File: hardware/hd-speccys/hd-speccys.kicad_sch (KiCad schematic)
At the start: 6 parts, among them J1 PI_ZERO_2x20, J2 ULA_ZX_02x20, J3 ULA_SOCKET_02x20, U1 74LS541, U2 74LS132, U3 74LS541

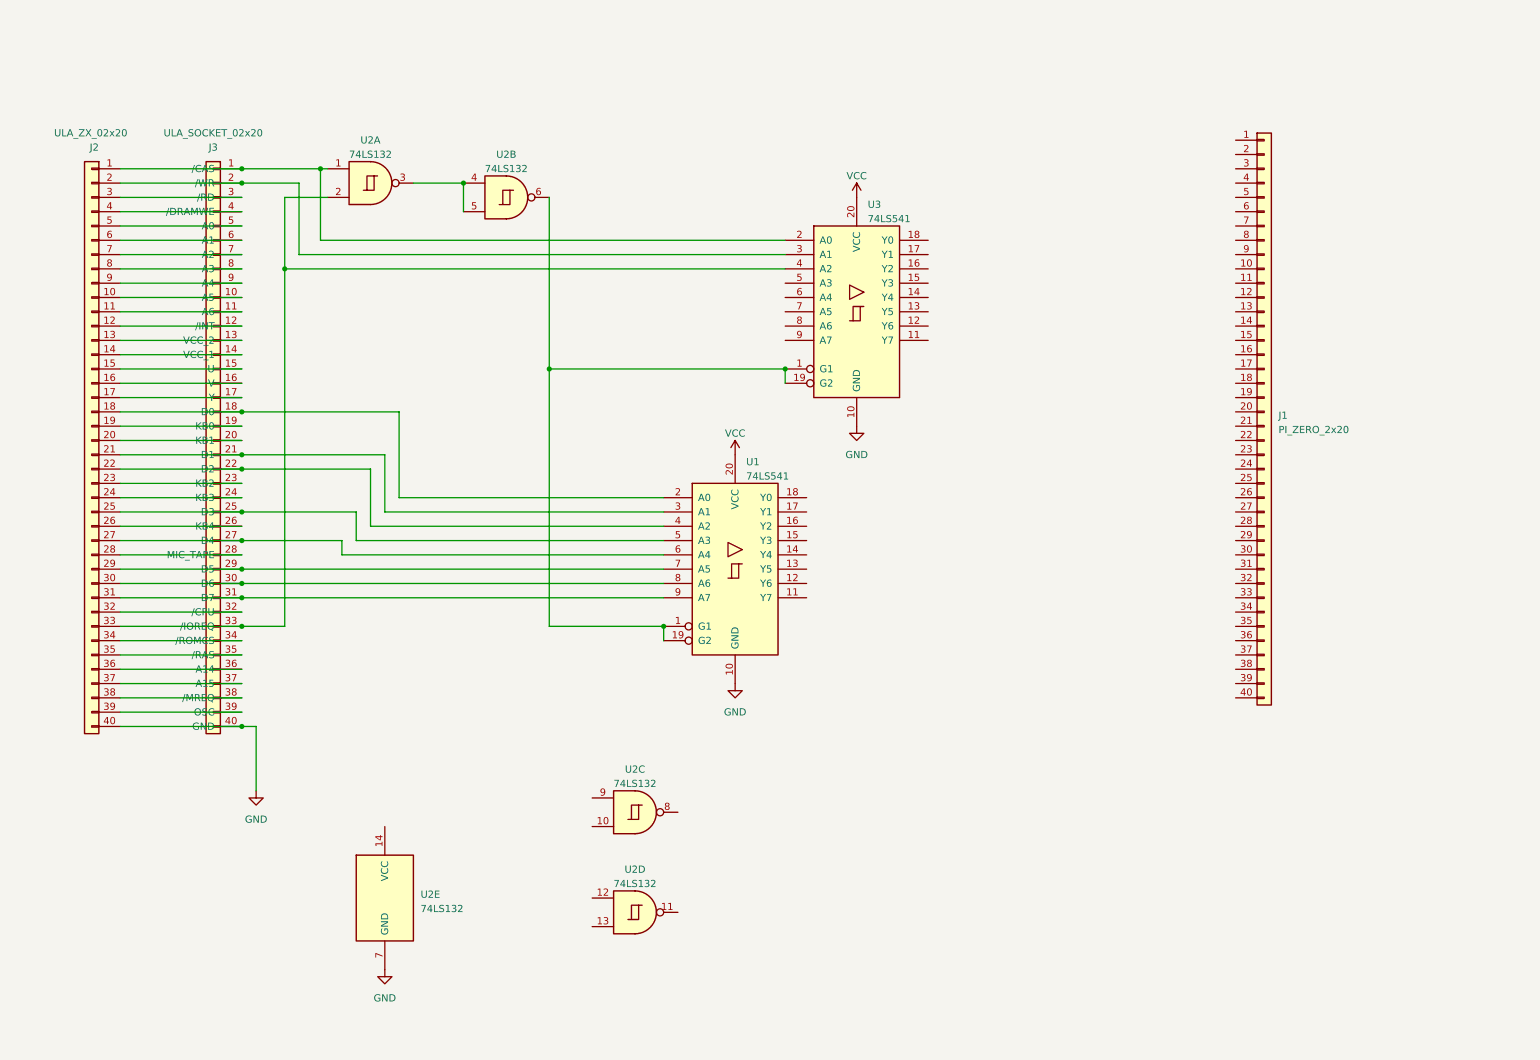
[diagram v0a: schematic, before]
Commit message: WE HAVE VIDEO (albeit quite corrupted!)
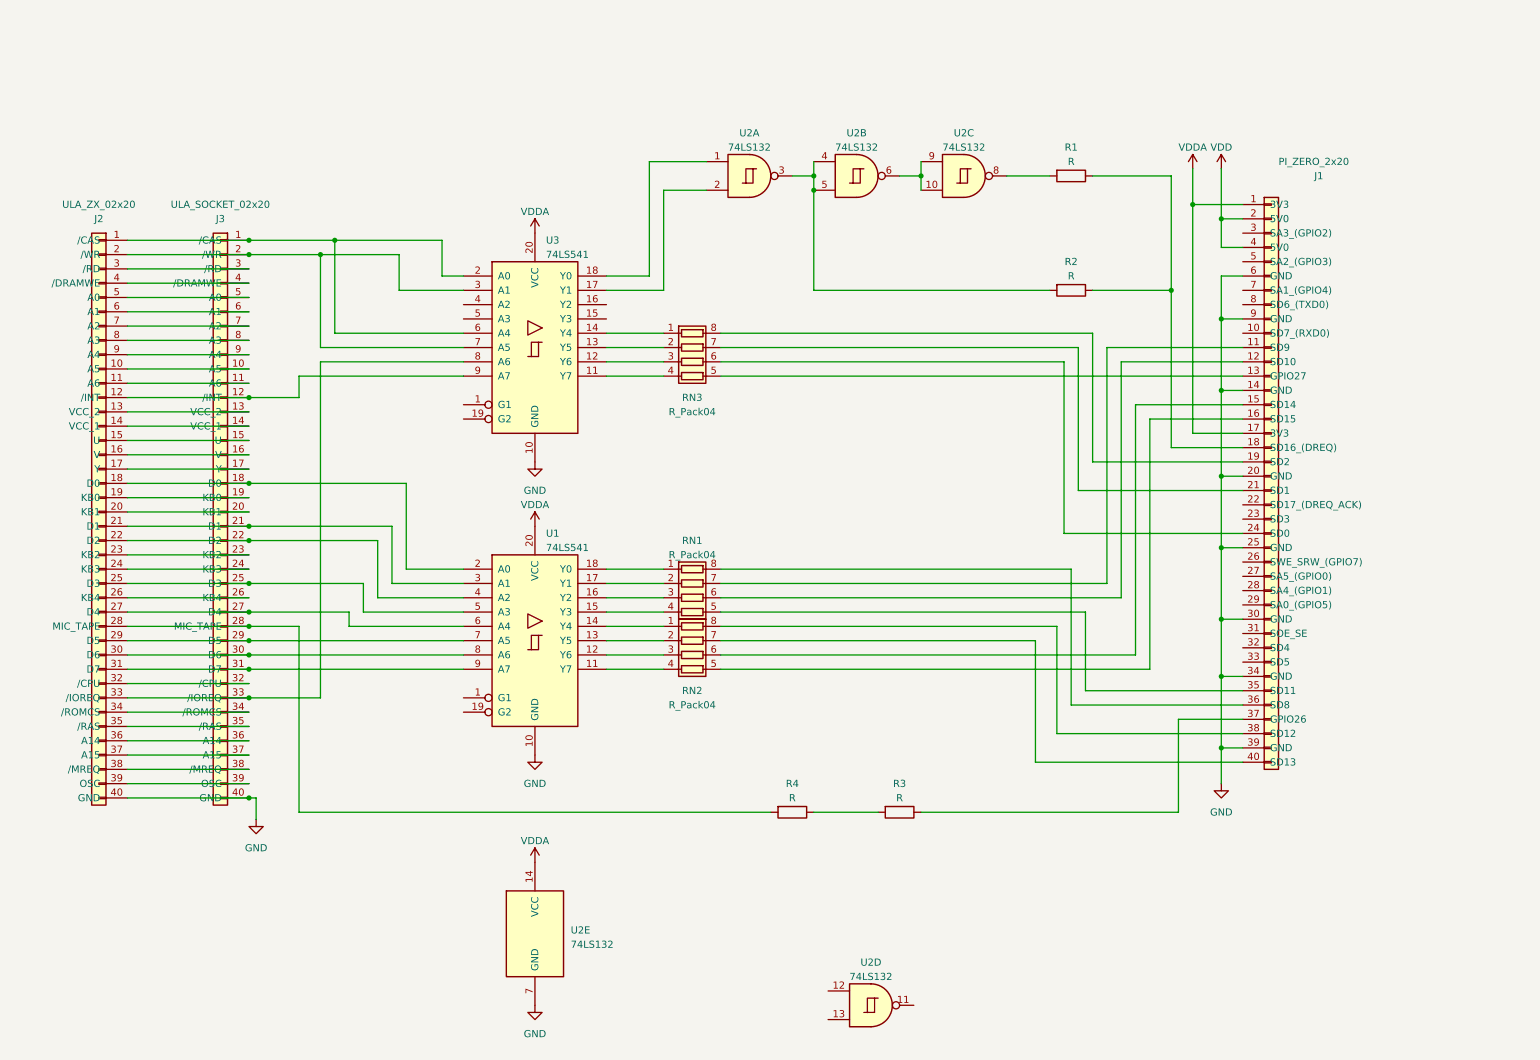
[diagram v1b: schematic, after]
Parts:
- added R1, R2, R3, R4: R, symbol Device:R
- added RN1, RN2, RN3: R_Pack04, symbol Device:R_Pack04
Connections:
- net VCC is gone; now on net VDDA: U1.20 (VCC), U3.20 (VCC)
- net GND: now also J1.14 (GND), J1.20 (GND), J1.25 (GND), J1.30 (GND), J1.34 (GND), J1.39 (GND), J1.6 (GND), J1.9 (GND)
- net at U3.11 (Y7): now also RN3.4 (R4.1)
- net at U3.12 (Y6): now also RN3.3 (R3.1)
- net at U3.13 (Y5): now also RN3.2 (R2.1)
- net at U3.14 (Y4): now also RN3.1 (R1.1)
- net at U3.17 (Y1): now also U2.2
- net at U3.18 (Y0): now also U2.1
- net at J2.1 (/CAS), J3.1 (/CAS), U3.2 (A0): now also U3.6 (A4); no longer U2.1
- net at J2.2 (/WR), J3.2 (/WR), U3.3 (A1): now also U3.7 (A5)
- net at J2.33 (/IOREQ), J3.33 (/IOREQ): now also U3.8 (A6); no longer U2.2, U3.4 (A2)
- net at U3.9 (A7): now also J2.12 (/INT), J3.12 (/INT)
- net at J2.28 (MIC_TAPE), J3.28 (MIC_TAPE): now also R4.2
- net at U2.10: now also U2.6, U2.9
- net at U2.8: now also R1.2
- net at U2.3, U2.4, U2.5: now also R2.2
- net VDDA: now reaches U2.14 (VCC)
- net VDDA: now also J1.1 (3V3), J1.17 (3V3)
- net at J1.11 (SD9): now also RN1.7 (R2.2)
- net at J1.12 (SD10): now also RN1.6 (R3.2)
- net at J1.13 (GPIO27): now also RN3.5 (R4.2)
- net at J1.15 (SD14): now also RN2.6 (R3.2)
- net at J1.16 (SD15): now also RN2.5 (R4.2)
- net at J1.18 (SD16_(DREQ)): now also R1.1, R2.1
- net at J1.19 (SD2): now also RN3.8 (R1.2)
- net VDD: now reaches J1.2 (5V0)
- net VDD: now also J1.4 (5V0)
- net at J1.21 (SD1): now also RN3.7 (R2.2)
- net at J1.24 (SD0): now also RN3.6 (R3.2)
- net at J1.35 (SD11): now also RN1.5 (R4.2)
- net at J1.36 (SD8): now also RN1.8 (R1.2)
- net at J1.37 (GPIO26): now also R3.1
- net at J1.38 (SD12): now also RN2.8 (R1.2)
- net at J1.40 (SD13): now also RN2.7 (R2.2)
- net at U1.11 (Y7): now also RN2.4 (R4.1)
- net at U1.12 (Y6): now also RN2.3 (R3.1)
- net at U1.13 (Y5): now also RN2.2 (R2.1)
- net at U1.14 (Y4): now also RN2.1 (R1.1)
- net at U1.15 (Y3): now also RN1.4 (R4.1)
- net at U1.16 (Y2): now also RN1.3 (R3.1)
- net at U1.17 (Y1): now also RN1.2 (R2.1)
- net at U1.18 (Y0): now also RN1.1 (R1.1)
- new net: R3.2, R4.1
- now unconnected: U1.1 (G1), U1.19 (G2), U3.1 (G1), U3.19 (G2)
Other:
- moved on the sheet: J3, U1, U2A, U2B, U2C, U2D, U2E, U3

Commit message: wip: PCB prototype/schematic
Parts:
- removed RN1, RN2, RN3: R_Pack04, symbol Device:R_Pack04
- removed U2: 74LS132, symbol 74xx:74LS132
- added C1: 100nF, Capacitor_SMD:C_0603_1608Metric_Pad1.08x0.95mm_HandSolder, symbol Device:C
- added C2, C3, C4, C5: C, Capacitor_SMD:C_0603_1608Metric_Pad1.08x0.95mm_HandSolder, symbol Device:C
- added D1, D2, D3: 1N4148, Diode_SMD:D_SOD-323_HandSoldering, symbol Diode:1N4148
- added J1: POWER 9-20VDC, Connector_PinHeader_2.54mm:PinHeader_1x02_P2.54mm_Horizontal, symbol Connector:Conn_01x02_Pin
- added J5: UART, Connector_PinHeader_2.54mm:PinHeader_1x03_P2.54mm_Vertical, symbol Connector:Conn_01x03_Pin
- added J6: Debug_Data, Connector_PinHeader_2.54mm:PinHeader_1x08_P2.54mm_Vertical, symbol Connector:Conn_01x08_Pin
- added J7: Debug_Ctrl, Connector_PinHeader_2.54mm:PinHeader_1x06_P2.54mm_Vertical, symbol Connector:Conn_01x06_Pin
- added R1, R10, R11, R12, R13, R14, R15, R16, R17, R18, R19, R2, R20, R21, R22, R23, R24, R25, R26, R27, R28, R3, R31, R34, R35, R5, R6, R7, R8, R9: R, Resistor_SMD:R_0603_1608Metric_Pad0.98x0.95mm_HandSolder, symbol Device:R
- added R32: 1k, Potentiometer_SMD:Potentiometer_Bourns_TC33X_Vertical, symbol Device:R_Variable
- added U3, U5: 74HC00, Package_SO:TSSOP-14_4.4x5mm_P0.65mm, symbol 74xx:74HC00
- added U4: TSR_1-2450, Converter_DCDC:Converter_DCDC_TRACO_TSR-1_THT, symbol Regulator_Switching:TSR_1-2450
- J2: renamed from J1; footprint (none) -> Module:Raspberry_Pi_Zero_Socketed_THT_FaceDown_MountingHoles
- J3: footprint (none) -> Package_DIP:DIP-40_W15.24mm_Socket
- J4: renamed from J2; footprint (none) -> Package_DIP:DIP-40_W15.24mm_Socket
- R29: renamed from R3; footprint (none) -> Resistor_SMD:R_0603_1608Metric_Pad0.98x0.95mm_HandSolder
- R30: renamed from R2; footprint (none) -> Resistor_SMD:R_0603_1608Metric_Pad0.98x0.95mm_HandSolder
- R33: renamed from R1; footprint (none) -> Resistor_SMD:R_0603_1608Metric_Pad0.98x0.95mm_HandSolder
- R4: footprint (none) -> Resistor_SMD:R_0603_1608Metric_Pad0.98x0.95mm_HandSolder
- U1: renamed from U3; footprint (none) -> Package_SO:TSSOP-20_4.4x6.5mm_P0.65mm
- U2: renamed from U1; footprint (none) -> Package_SO:TSSOP-20_4.4x6.5mm_P0.65mm
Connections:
- net GND: now also U1.1 (G1), U1.19 (G2), U2.1 (G1), U2.19 (G2), C2.2, C3.2, C4.2, C5.2, J1.2 (GND), J5.1 (GND), U3.7 (GND), U4.2 (GND), U5.7 (GND)
- net VDD: now also U4.3 (Vout)
- net VDDA: now also C2.1, C3.1, C4.1, C5.1, U3.14 (VCC), U5.14 (VCC)
- net at U1.14 (Y4): now also R18.2
- net at U1.13 (Y5): now also U3.2
- net at U1.12 (Y6): now also R19.2
- net at U1.11 (Y7): now also R20.2
- net at J2.13 (GPIO27): now also J7.1 (Pin_1), R20.1
- net at J2.24 (SD0): now also J7.4 (Pin_4), R19.1
- net at J2.21 (SD1): now also J7.2 (Pin_2), R18.1
- net at J2.19 (SD2): now also J7.3 (Pin_3), R17.1
- net at R29.2: now also J7.5 (Pin_5), U3.3; no longer R4.1
- net at J3.28 (MIC_TAPE), J4.28 (MIC_TAPE): now also C1.2; no longer R4.2
- net at U1.15 (Y3): now also U3.5
- net at U1.16 (Y2): now also R17.2
- net at U1.17 (Y1): now also U3.1
- net at U1.18 (Y0): now also U3.4
- net at J3.1 (/CAS), J4.1 (/CAS): now also R4.2, R5.2; no longer U1.2 (A0), U1.6 (A4)
- net at J3.2 (/WR), J4.2 (/WR): now also R6.2, R7.2; no longer U1.3 (A1), U1.7 (A5)
- net at U1.4 (A2): now also R3.1
- net at U1.5 (A3): now also R4.1
- net at J3.33 (/IOREQ), J4.33 (/IOREQ): now also R1.2, R2.2, R3.2; no longer U1.8 (A6)
- net at J3.12 (/INT), J4.12 (/INT): now also R8.2; no longer U1.9 (A7)
- net at U2.18 (Y0): now also R21.2
- net at U2.17 (Y1): now also R22.2
- net at U2.16 (Y2): now also R23.2
- net at U2.15 (Y3): now also R24.2
- net at J2.35 (SD11): now also J6.5 (Pin_5), R25.1
- net at J2.12 (SD10): now also J6.6 (Pin_6), R26.1
- net at J2.11 (SD9): now also J6.7 (Pin_7), R27.1
- net at J2.36 (SD8): now also J6.8 (Pin_8), R28.1
- net at J3.18 (D0), J4.18 (D0): now also R9.2; no longer U2.2 (A0)
- net at J3.21 (D1), J4.21 (D1): now also R10.2; no longer U2.3 (A1)
- net at J3.22 (D2), J4.22 (D2): now also R11.2; no longer U2.4 (A2)
- net at J3.25 (D3), J4.25 (D3): now also R12.2; no longer U2.5 (A3)
- net at J3.27 (D4), J4.27 (D4): now also R13.2; no longer U2.6 (A4)
- net at J3.29 (D5), J4.29 (D5): now also R14.2; no longer U2.7 (A5)
- net at J3.30 (D6), J4.30 (D6): now also R15.2; no longer U2.8 (A6)
- net at J3.31 (D7), J4.31 (D7): now also R16.2; no longer U2.9 (A7)
- net at J2.18 (SD16_(DREQ)), R30.1, R33.1: now also R34.1, R35.1
- net at R33.2: now also U3.11, U5.1, U5.2
- net at R30.2: now also J7.6 (Pin_6), U3.10, U3.6, U3.9
- net at U2.14 (Y4): now also R25.2
- net at U2.13 (Y5): now also R26.2
- net at U2.12 (Y6): now also R27.2
- net at U2.11 (Y7): now also R28.2
- net at J2.16 (SD15): now also J6.1 (Pin_1), R21.1
- net at J2.15 (SD14): now also J6.2 (Pin_2), R22.1
- net at J2.40 (SD13): now also J6.3 (Pin_3), R23.1
- net at J2.38 (SD12): now also J6.4 (Pin_4), R24.1
- net at J2.10 (SD7_(RXD0)): now also J5.3 (RXD)
- net at J2.26 (SWE_SRW_(GPIO7)): now also D3.2 (A)
- net at J2.8 (SD6_(TXD0)): now also J5.2 (TXD)
- new net: J1.1 (VCC), U4.1 (Vin)
- new net: D2.2 (A), D3.1 (K)
- new net: R6.1, U1.7 (A5)
- new net: R34.2, U5.10, U5.6, U5.9
- new net: U5.12, U5.13, U5.8
- new net: R2.1, U1.3 (A1)
- new net: R35.2, U5.11
- new net: R5.1, U1.6 (A4)
- new net: R10.1, U2.3 (A1)
- new net: R31.1, R32.2
- new net: C1.1, R31.2
- new net: R1.1, U1.2 (A0)
- new net: R7.1, U1.8 (A6)
- new net: R8.1, U1.9 (A7)
- new net: D1.1 (K), R32.1
- new net: R15.1, U2.8 (A6)
- new net: R9.1, U2.2 (A0)
- new net: R16.1, U2.9 (A7)
- new net: U5.3, U5.4, U5.5
- new net: R11.1, U2.4 (A2)
- new net: R14.1, U2.7 (A5)
- new net: R13.1, U2.6 (A4)
- new net: D1.2 (A), D2.1 (K)
- new net: R12.1, U2.5 (A3)
- new net: U3.12, U3.13, U3.8
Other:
- moved on the sheet: J2, J3, J4, R29, R30, R33, U1, U2

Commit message: hw: schematic updates
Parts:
- removed C5: C, Capacitor_SMD:C_0603_1608Metric_Pad1.08x0.95mm_HandSolder, symbol Device:C
- removed R33, R34, R35: R, Resistor_SMD:R_0603_1608Metric_Pad0.98x0.95mm_HandSolder, symbol Device:R
- removed U3, U5: 74HC00, Package_SO:TSSOP-14_4.4x5mm_P0.65mm, symbol 74xx:74HC00
- added U3: 74LS10, Package_SO:TSSOP-14_4.4x5mm_P0.65mm, symbol 74xx:74LS10
- added U5: 74AHC1G32, Package_TO_SOT_SMD:SOT-353_SC-70-5_Handsoldering, symbol 74xGxx:74AHC1G32
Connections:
- net GND: now also U1.2 (A0), U3.7 (GND), U5.3 (GND)
- net VDDA: now also U3.14 (VCC), U5.5 (VCC)
- net at J3.33 (/IOREQ), J4.33 (/IOREQ), R2.2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: no longer R1.2
- net at J2.18 (SD16_(DREQ)), R30.1: now also J7.1 (Pin_1), R1.1
- net at J2.13 (GPIO27), R20.1: now also J7.6 (Pin_6); no longer J7.1 (Pin_1)
- net at J2.21 (SD1), R18.1: now also J7.4 (Pin_4); no longer J7.2 (Pin_2)
- net at J2.24 (SD0), R19.1: now also J7.5 (Pin_5); no longer J7.4 (Pin_4)
- net at R29.2: now also J7.2 (Pin_2), U5.4; no longer J7.5 (Pin_5)
- net at R30.2: now also U3.12, U3.3, U3.4, U3.5; no longer J7.6 (Pin_6)
- net at R20.2, U1.11 (Y7): now also U3.13
- net at U1.13 (Y5): now also U5.2
- net at U1.15 (Y3): now also U3.2
- net at U1.17 (Y1): now also U3.1, U5.1
- new net: R1.2, U3.8
- new net: U3.10, U3.11, U3.6, U3.9
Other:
- moved on the sheet: R17, R18, R19, R20, R29, R30

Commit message: hw: Finished silkscreen
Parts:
- added J8: GND, Connector_PinHeader_2.54mm:PinHeader_1x01_P2.54mm_Vertical, symbol Connector:Conn_01x01_Pin
- J2: value PI_ZERO_2x20 -> PI_ZERO
- J3: value ULA_SOCKET_02x20 -> ULA_SOCKET
- J4: value ULA_ZX_02x20 -> ULA_ZX
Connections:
- net GND: now also J8.1 (Pin_1)
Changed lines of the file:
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@@
     (stroke (width 0) (type default))
   )
-  (wire (pts (xy 177.8 20.32) (xy 177.8 21.59))
+  (wire (pts (xy 177.8 20.32) (xy 177.8 22.86))
     (stroke (width 0) (type default))
   )
@@
     (stroke (width 0) (type default))
   )
-  (wire (pts (xy 177.8 21.59) (xy 179.07 21.59))
-    (stroke (width 0) (type default))
-  )
   (wire (pts (xy 35.56 92.71) (xy 57.15 92.71))
     (stroke (width 0) (type default))
@@
     (stroke (width 0) (type default))
   )
-  (wire (pts (xy 177.8 22.86) (xy 179.07 22.86))
-    (stroke (width 0) (type default))
-  )
-  (wire (pts (xy 179.07 21.59) (xy 179.07 22.86))
-    (stroke (width 0) (type default))
-  )
   (wire (pts (xy 57.15 133.35) (xy 87.63 133.35))
     (stroke (width 0) (type default))
@@
   (wire (pts (xy 85.09 64.77) (xy 85.09 67.31))
     (stroke (width 0) (type default))
+  )
+  (symbol (lib_id "power:GND") (at 88.9 29.21 0) (unit 1)
+    (in_bom yes) (on_board yes) (dnp no) (fields_autoplaced)
+    (property "Reference" "#PWR017" (at 88.9 35.56 0)
+      (effects (font (size 1.27 1.27)) hide)
+    )
+    (property "Value" "GND" (at 88.9 34.29 0)
+      (effects (font (size 1.27 1.27)))
+    )
+    (property "Footprint" "" (at 88.9 29.21 0)
+      (effects (font (size 1.27 1.27)) hide)
+    )
+    (property "Datasheet" "" (at 88.9 29.21 0)
+      (effects (font (size 1.27 1.27)) hide)
+    )
+    (pin "1")
+    (instances
+      (project "hd-speccys"
+        (path "/d655584b-1b0c-4d69-832c-956bfbc09454"
+          (reference "#PWR017") (unit 1)
+        )
+      )
+    )
   )
   (symbol (lib_id "Regulator_Switching:TSR_1-2450") (at 48.26 180.34 0) (unit 1)
@@
   (symbol (lib_id "Connector:Conn_01x08_Pin") (at 162.56 100.33 0) (mirror y) (unit 1)
     (in_bom yes) (on_board yes) (dnp no)
-    (property "Reference" "J6" (at 168.91 99.06 0)
-      (effects (font (size 1.27 1.27)))
-    )
-    (property "Value" "Debug_Data" (at 168.91 101.6 0)
+    (property "Reference" "J6" (at 162.56 87.63 0)
+      (effects (font (size 1.27 1.27)))
+    )
+    (property "Value" "Debug_Data" (at 154.94 87.63 0)
       (effects (font (size 1.27 1.27)))
     )
@@
   (symbol (lib_id "Connector:Conn_01x06_Pin") (at 207.01 83.82 0) (mirror y) (unit 1)
     (in_bom yes) (on_board yes) (dnp no)
-    (property "Reference" "J7" (at 212.09 82.55 0)
-      (effects (font (size 1.27 1.27)))
-    )
-    (property "Value" "Debug_Ctrl" (at 212.09 85.09 0)
+    (property "Reference" "J7" (at 208.28 95.25 0)
+      (effects (font (size 1.27 1.27)))
+    )
+    (property "Value" "Debug_Ctrl" (at 200.66 95.25 0)
       (effects (font (size 1.27 1.27)))
     )
@@
         (path "/d655584b-1b0c-4d69-832c-956bfbc09454"
           (reference "#PWR016") (unit 1)
+        )
+      )
+    )
+  )
+  (symbol (lib_id "Connector:Conn_01x01_Pin") (at 83.82 29.21 0) (unit 1)
+    (in_bom yes) (on_board yes) (dnp no) (fields_autoplaced)
+    (property "Reference" "J8" (at 84.455 25.4 0)
+      (effects (font (size 1.27 1.27)))
+    )
+    (property "Value" "GND" (at 84.455 27.94 0)
+      (effects (font (size 1.27 1.27)))
+    )
+    (property "Footprint" "Connector_PinHeader_2.54mm:PinHeader_1x01_P2.54mm_Vertical" (at 83.82 29.21 0)
+      (effects (font (size 1.27 1.27)) hide)
+    )
+    (property "Datasheet" "~" (at 83.82 29.21 0)
+      (effects (font (size 1.27 1.27)) hide)
+    )
+    (pin "1")
+    (instances
+      (project "hd-speccys"
+        (path "/d655584b-1b0c-4d69-832c-956bfbc09454"
+          (reference "J8") (unit 1)
         )
       )
@@
       (effects (font (size 1.27 1.27)))
     )
-    (property "Value" "ULA_SOCKET_02x20" (at 52.07 50.8 0)
+    (property "Value" "ULA_SOCKET" (at 52.07 50.8 0)
       (effects (font (size 1.27 1.27)))
     )
@@
       (effects (font (size 1.27 1.27)))
     )
-    (property "Value" "ULA_ZX_02x20" (at 30.48 50.8 0)
+    (property "Value" "ULA_ZX" (at 30.48 50.8 0)
       (effects (font (size 1.27 1.27)))
     )
@@
   (symbol (lib_name "Conn_01x40_2") (lib_id "Connector_Generic:Conn_01x40") (at 264.16 99.06 0) (unit 1)
     (in_bom yes) (on_board yes) (dnp no)
-    (property "Reference" "J2" (at 266.7 45.72 0)
+    (property "Reference" "J2" (at 262.89 45.72 0)
       (effects (font (size 1.27 1.27)) (justify left))
     )
-    (property "Value" "PI_ZERO_2x20" (at 260.35 43.18 0)
+    (property "Value" "PI_ZERO" (at 260.35 43.18 0)
       (effects (font (size 1.27 1.27)) (justify left))
     )
